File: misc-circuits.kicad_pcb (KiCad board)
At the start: 6 copper layers, 30 parts, among them U1 Value

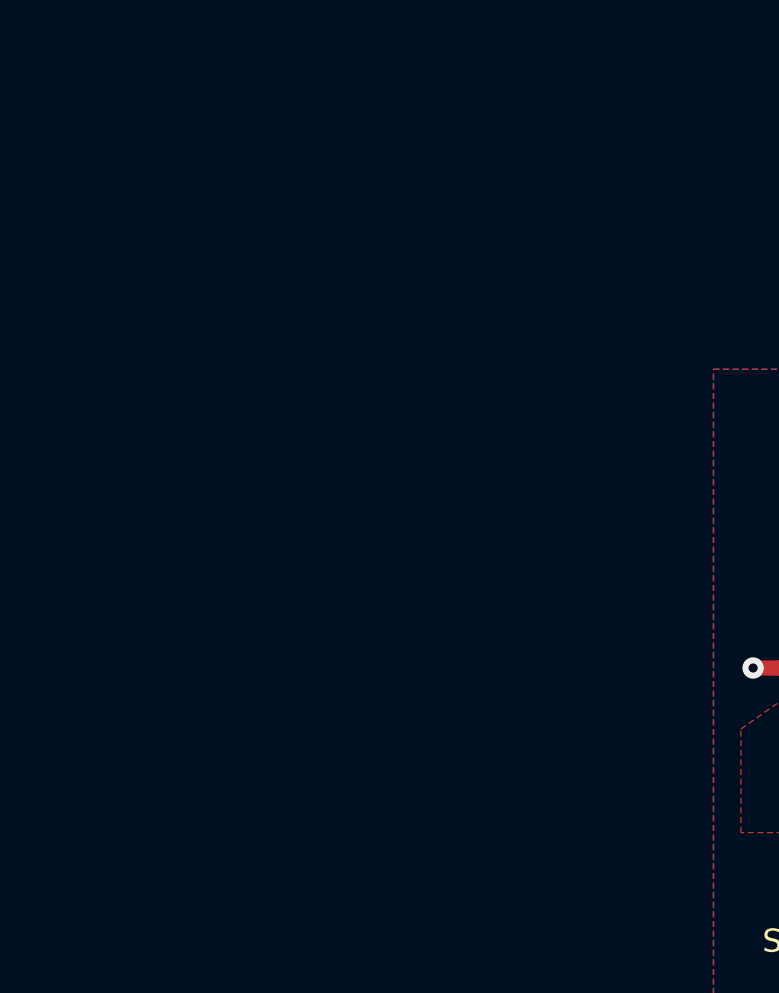
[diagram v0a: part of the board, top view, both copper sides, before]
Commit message: added preliminary burn wire circuit, flat flex cable, and sun sensor *layout is not complete*
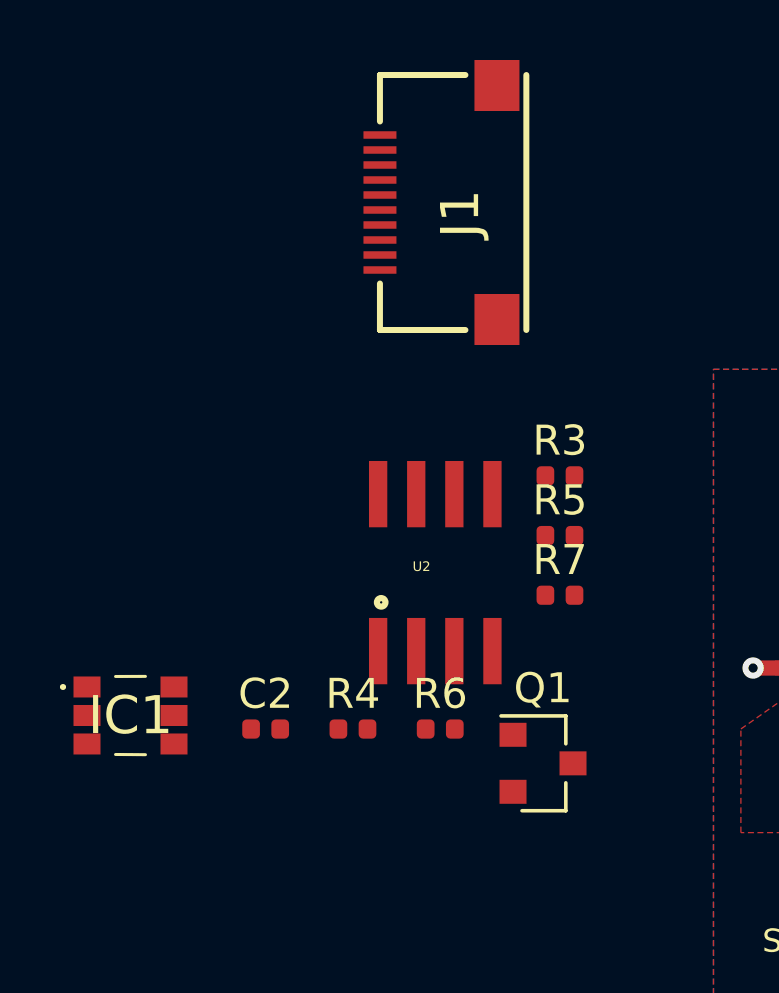
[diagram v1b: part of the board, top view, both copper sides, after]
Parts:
- added C2: 0.1uF, Capacitor_SMD:C_0402_1005Metric, F.Cu at (114.4, 106.6)
- added IC1: TSL2561, misc-circuits:TSL2561, F.Cu at (109.9, 106.1)
- added J1: XF2M-1015-1A, custom-footprints:XF2M-1015-1A, F.Cu at (118.2, 89.0)
- added Q1: IRLML2803, Package_TO_SOT_SMD:SOT-23, F.Cu at (123.6, 107.7)
- added R3: 10k, Resistor_SMD:R_0402_1005Metric, F.Cu at (124.2, 98.1)
- added R4: 4.7k, Resistor_SMD:R_0402_1005Metric, F.Cu at (117.3, 106.6)
- added R5: 100k, Resistor_SMD:R_0402_1005Metric, F.Cu at (124.2, 100.1)
- added R6: 0, Resistor_SMD:R_0402_1005Metric, F.Cu at (120.2, 106.6)
- added R7: 0, Resistor_SMD:R_0402_1005Metric, F.Cu at (124.2, 102.1)
- added U2: NDS8434, custom-footprints:NDS8434, F.Cu at (120.1, 101.4)
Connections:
- net +3.3V renamed +3V3
